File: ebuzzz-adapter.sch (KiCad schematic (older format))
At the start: 34 parts, among them J1 Conn_01x04, J2 Conn_01x04, J3 Conn_01x06, J4 EBUS, Q1 BC817-40, U1 CNY17-4, U2 CNY17-4, U3 LM2903DT, U4 LP2951-50DR

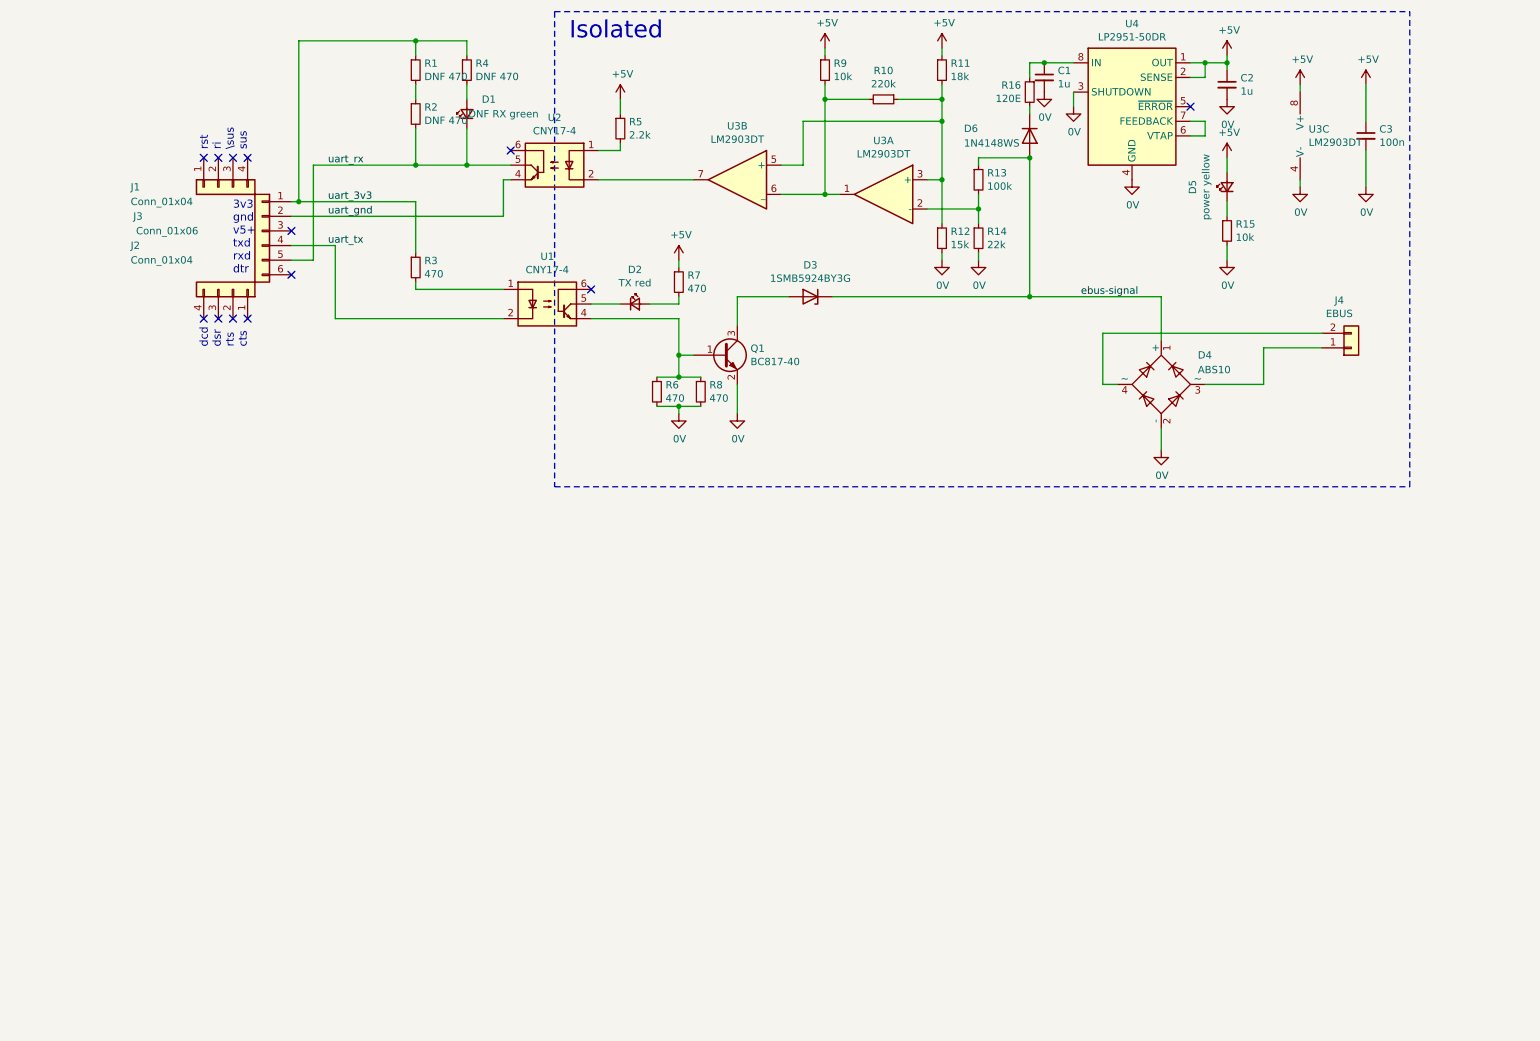
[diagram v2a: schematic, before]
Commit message: replace external board with onboard CP2104
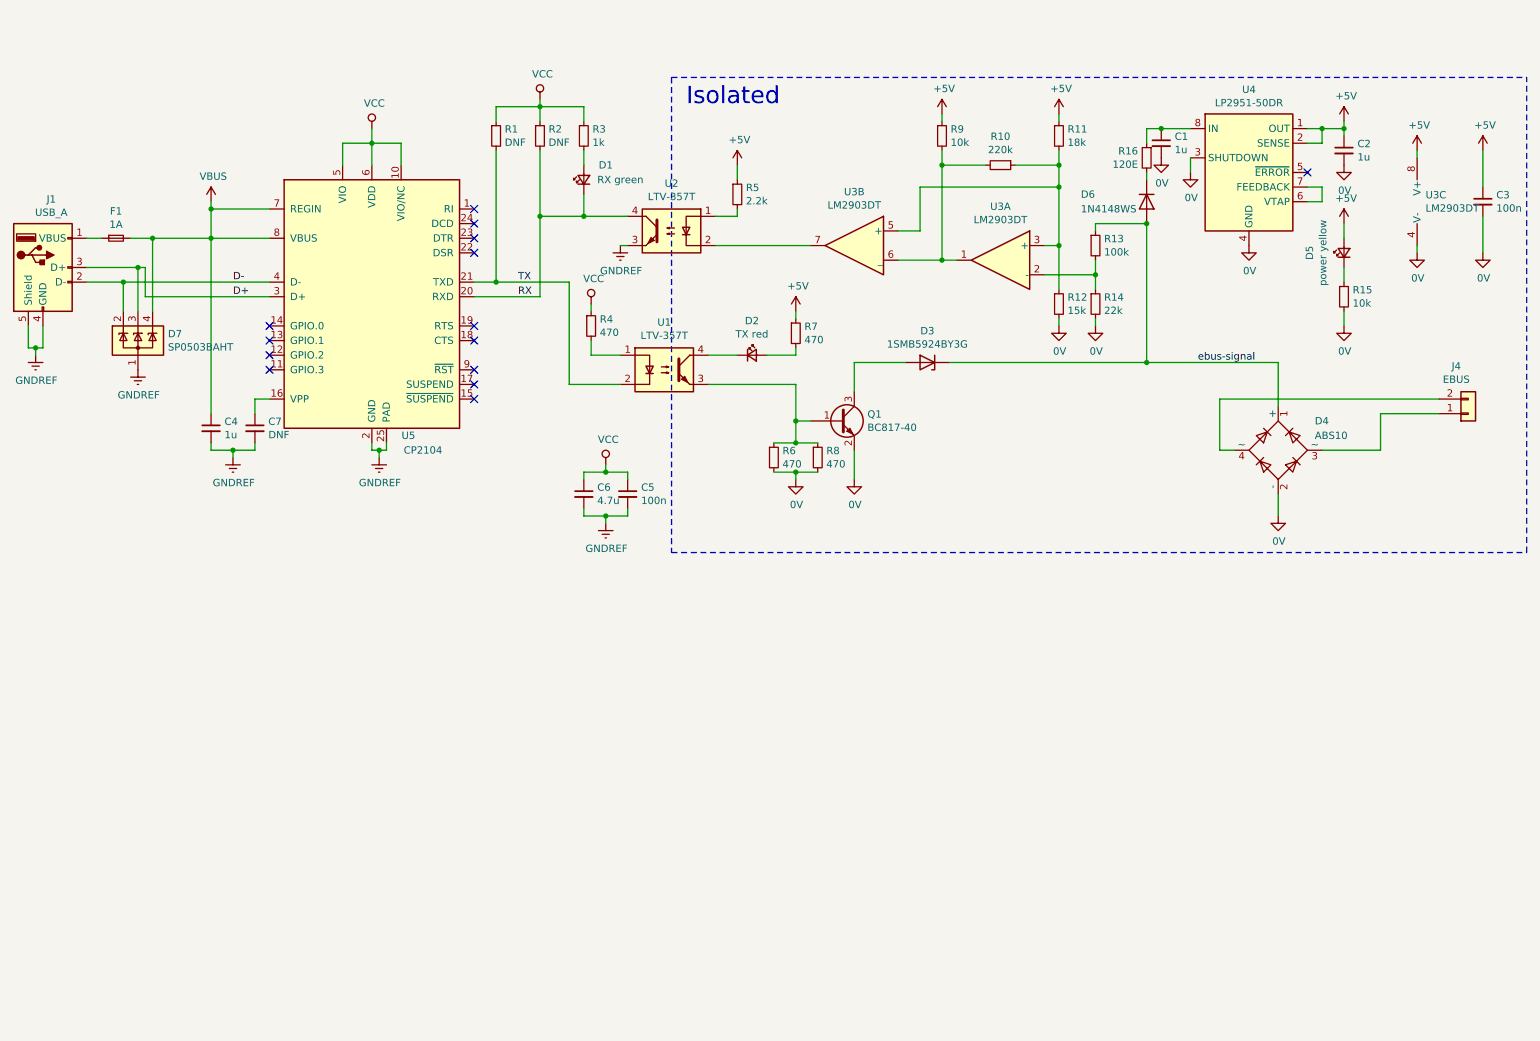
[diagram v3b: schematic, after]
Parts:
- removed J1, J2: Conn_01x04, Connector_PinHeader_2.54mm:PinHeader_1x04_P2.54mm_Vertical, symbol Connector_Generic:Conn_01x04
- removed J3: Conn_01x06, Connector_PinHeader_2.54mm:PinHeader_1x06_P2.54mm_Vertical, symbol Connector_Generic:Conn_01x06
- removed R4: DNF 470, Resistor_SMD:R_0805_2012Metric_Pad1.15x1.40mm_HandSolder, symbol Device:R_Small
- removed U1, U2: CNY17-4, Package_DIP:DIP-6_W7.62mm, symbol Isolator:CNY17-4
- added C4: 1u, Capacitor_SMD:C_0805_2012Metric, symbol Device:C_Small
- added C5: 100n, Capacitor_SMD:C_0805_2012Metric, symbol Device:C_Small
- added C6: 4.7u, Capacitor_SMD:C_0805_2012Metric, symbol Device:C_Small
- added C7: DNF, Capacitor_SMD:C_0805_2012Metric, symbol Device:C_Small
- added D7: SP0503BAHT, Package_TO_SOT_SMD:SOT-143, symbol Power_Protection:SP0503BAHT
- added F1: 1A, Fuse:Fuse_1206_3216Metric, symbol Device:Fuse_Small
- added J1: USB_A, Connector_USB:USB_A_CNCTech_1001-011-01101_Horizontal, symbol Connector:USB_A
- added R3: 1k, Resistor_SMD:R_0805_2012Metric, symbol Device:R_Small
- added U1, U2: LTV-357T, Package_SO:SO-4_4.4x3.6mm_P2.54mm, symbol Isolator:LTV-357T
- added U5: CP2104, Package_DFN_QFN:QFN-24-1EP_4x4mm_P0.5mm_EP2.6x2.6mm_ThermalVias, symbol Interface_USB:CP2104
- C1, C2, C3: footprint Capacitor_SMD:C_0805_2012Metric_Pad1.15x1.40mm_HandSolder -> Capacitor_SMD:C_0805_2012Metric
- D1: value DNF RX green -> RX green; footprint LED_SMD:LED_0805_2012Metric_Pad1.15x1.40mm_HandSolder -> LED_SMD:LED_0805_2012Metric; LCSC (none) -> C2297
- D2, D5: footprint LED_SMD:LED_0805_2012Metric_Pad1.15x1.40mm_HandSolder -> LED_SMD:LED_0805_2012Metric
- J4: Farnell (none) -> 2008015
- R1, R2: value DNF 470 -> DNF; footprint Resistor_SMD:R_0805_2012Metric_Pad1.15x1.40mm_HandSolder -> Resistor_SMD:R_0805_2012Metric
- R10, R11, R12, R13, R15, R16, R5, R6, R7, R8, R9: footprint Resistor_SMD:R_0805_2012Metric_Pad1.15x1.40mm_HandSolder -> Resistor_SMD:R_0805_2012Metric
- R14: footprint Resistor_SMD:R_0805_2012Metric_Pad1.15x1.40mm_HandSolder -> Resistor_SMD:R_0805_2012Metric; LCSC C17475 -> C17560
- R4: renamed from R3; footprint Resistor_SMD:R_0805_2012Metric_Pad1.15x1.40mm_HandSolder -> Resistor_SMD:R_0805_2012Metric
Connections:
- net at R5.2: now also U2.1
- net at U3.7: now also U2.2
- net at R4.2: now also U1.1
- net at Q1.1 (B), R6.1, R8.1: now also U1.3
- net at D2.1 (K): now also U1.4
- net at D1.2 (A): now also R3.2
- net TX: now reaches R1.2
- net TX: now also U1.2, U5.21 (TXD); no longer R2.1
- net uart_3v3 renamed VCC
- net VCC: now also R2.1, C5.1, C6.1, R3.1, U5.10 (VIO/NC), U5.5 (VIO), U5.6 (VDD)
- net uart_rx renamed RX
- net RX: now also U2.4, U5.20 (RXD)
- new net: C7.1, U5.16 (VPP)
- new net: F1.1, J1.1 (VBUS)
- new net D+: D7.3 (K), J1.3 (D+), U5.3 (D+)
- new net D-: D7.2 (K), J1.2 (D-), U5.4 (D-)
- new net GNDREF: C4.2, C5.2, C6.2, C7.2, D7.1 (A), J1.4 (GND), J1.5 (Shield), U2.3, U5.2 (GND), U5.25 (PAD)
- new net VBUS: C4.1, D7.4 (K), F1.2, U5.7 (REGIN), U5.8 (VBUS)
- no-connect marks 13 -> 14
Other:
- note removed: "3v3\ngnd\nv5+\ntxd\nrxd\ndtr"
- note removed: "dcd\ndsr\nrts\ncts"
- note removed: "rst\nri\n\sus\nsus"
- moved on the sheet: C1, C2, C3, D1, D2, D3, D4, D5, D6, J4, Q1, R1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

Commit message: added manufacturing files
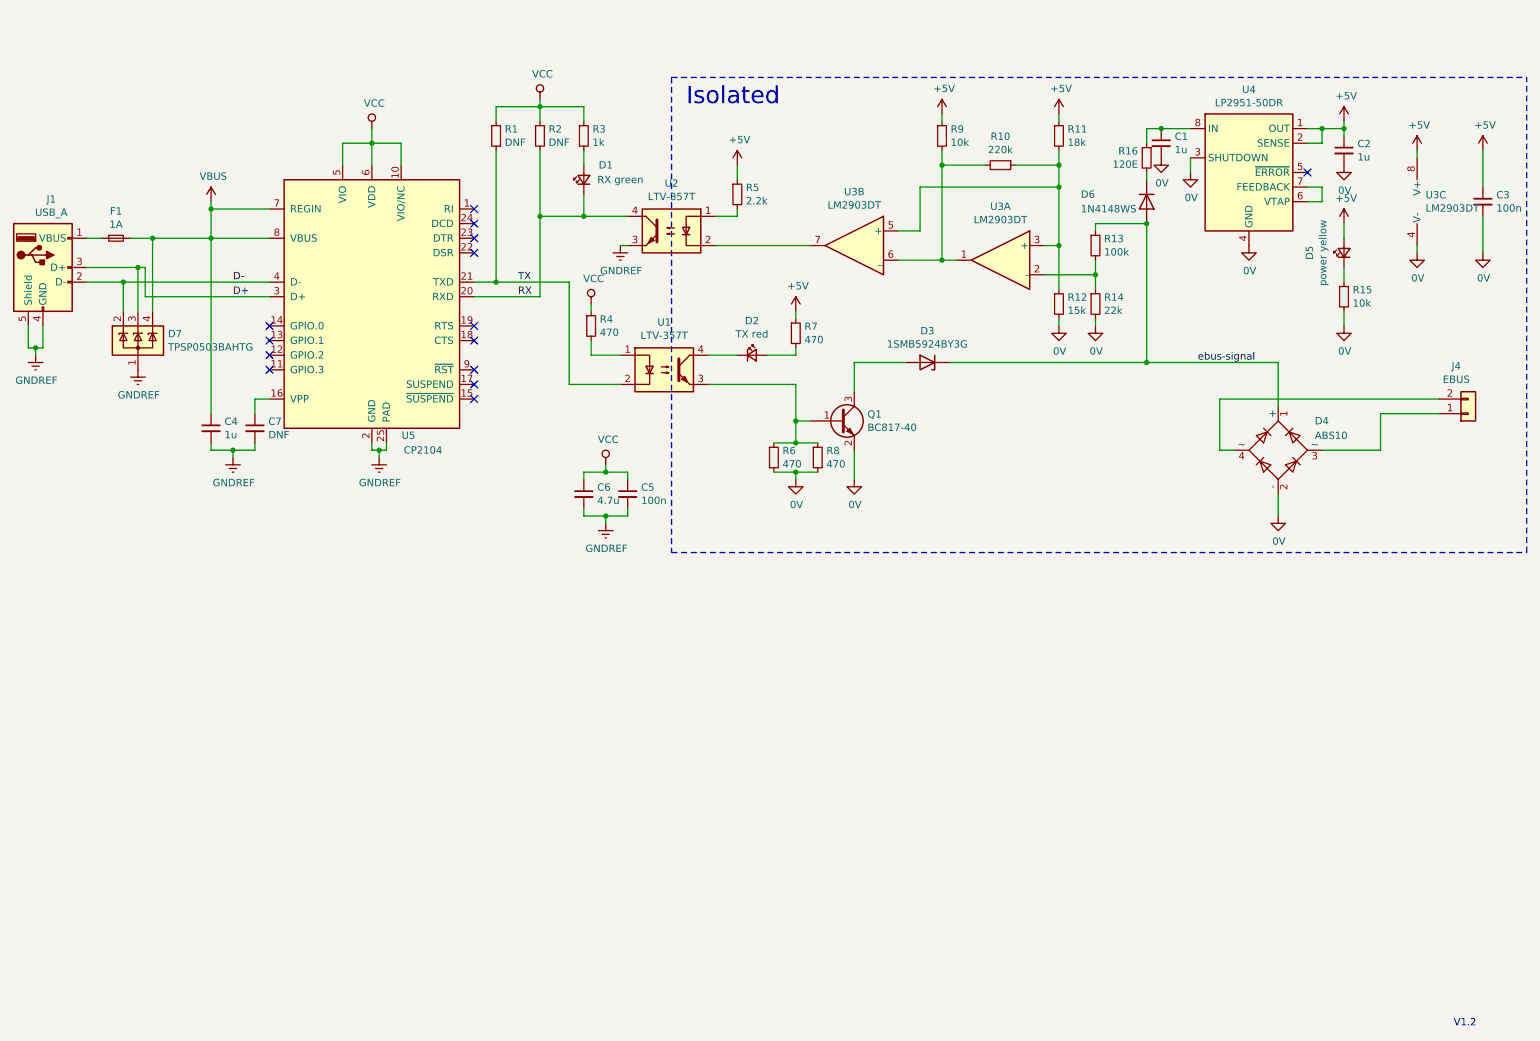
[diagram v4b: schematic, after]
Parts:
- D7: value SP0503BAHT -> TPSP0503BAHTG; LCSC C7074 -> C2682275
- J1: footprint Connector_USB:USB_A_CNCTech_1001-011-01101_Horizontal -> ebuzzz-adapter:XKB_Connectivity_U217-041N-4BV81; LCSC (none) -> C319178
- J4: Farnell 2008015 -> (none); LCSC (none) -> C69811
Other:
- note added: "V1.2"
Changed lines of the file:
@@
 F 2 "Connector_Phoenix_MC:PhoenixContact_MC_1,5_2-G-3.81_1x02_P3.81mm_Horizontal" H 10700 3450 50  0001 C CNN
 F 3 "~" H 10700 3450 50  0001 C CNN
-F 4 "2008015" H 10700 3450 50  0001 C CNN "Farnell"
+F 4 "C69811" H 10700 3450 50  0001 C CNN "LCSC"
 	1    10700 3450
 	1    0    0    1
@@
 F 0 "J1" H 1007 2917 50  0000 C CNN
 F 1 "USB_A" H 1007 2826 50  0000 C CNN
-F 2 "Connector_USB:USB_A_CNCTech_1001-011-01101_Horizontal" H 1100 2400 50  0001 C CNN
+F 2 "ebuzzz-adapter:XKB_Connectivity_U217-041N-4BV81" H 1100 2400 50  0001 C CNN
 F 3 " ~" H 1100 2400 50  0001 C CNN
+F 4 "C319178" H 950 2450 50  0001 C CNN "LCSC"
 	1    950  2450
 	1    0    0    -1
@@
 P 1600 2950
 F 0 "D7" H 1805 2996 50  0000 L CNN
-F 1 "SP0503BAHT" H 1805 2905 50  0000 L CNN
+F 1 "TPSP0503BAHTG" H 1805 2905 50  0000 L CNN
 F 2 "Package_TO_SOT_SMD:SOT-143" H 1825 2900 50  0001 L CNN
 F 3 "http://www.littelfuse.com/~/media/files/littelfuse/technical%20resources/documents/data%20sheets/sp05xxba.pdf" H 1725 3075 50  0001 C CNN
-F 4 "C7074" H 1600 2950 50  0001 C CNN "LCSC"
+F 4 "C2682275" H 1600 2950 50  0001 C CNN "LCSC"
 	1    1600 2950
 	1    0    0    -1
@@
 	1    0    0    -1
 $EndComp
+Text Notes 10600 7650 0    50   ~ 0
+V1.2
 $EndSCHEMATC
